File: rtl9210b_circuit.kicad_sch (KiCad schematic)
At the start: 45 parts, among them U1 RTL9210B-CG, U2 W25Q128JVSIQTR, U3 ETA3521FSG_C22362743, X1 X322525MOB4SI

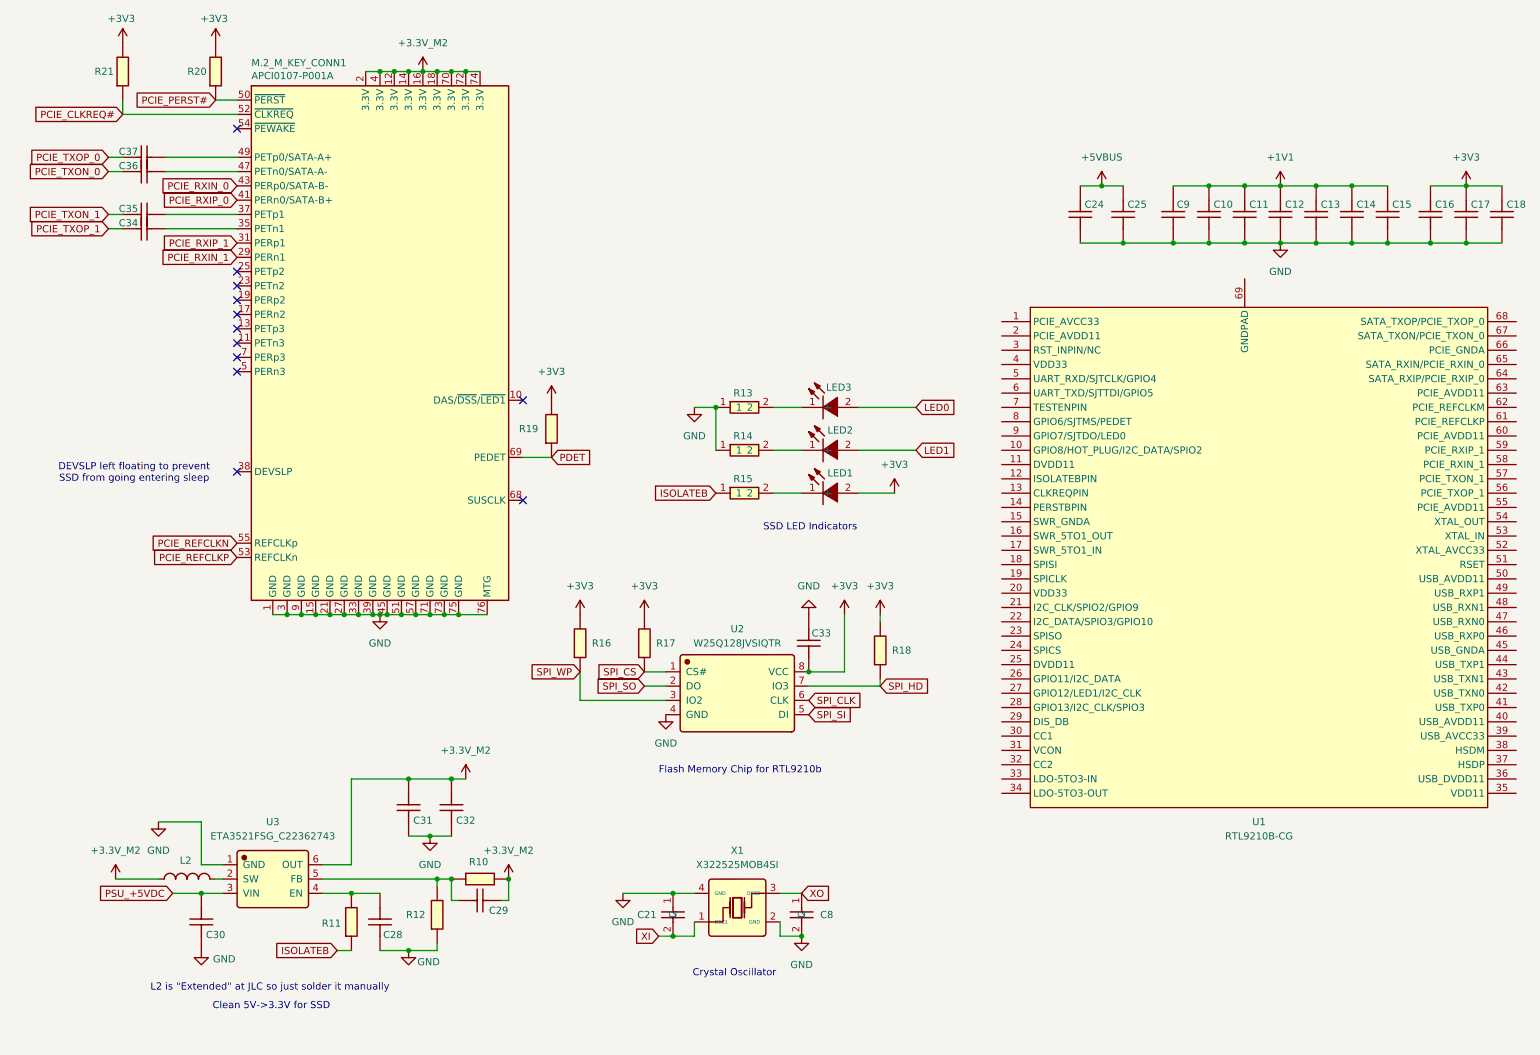
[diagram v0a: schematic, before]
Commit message: Preliminary design of RTL9210b SSD subsystem
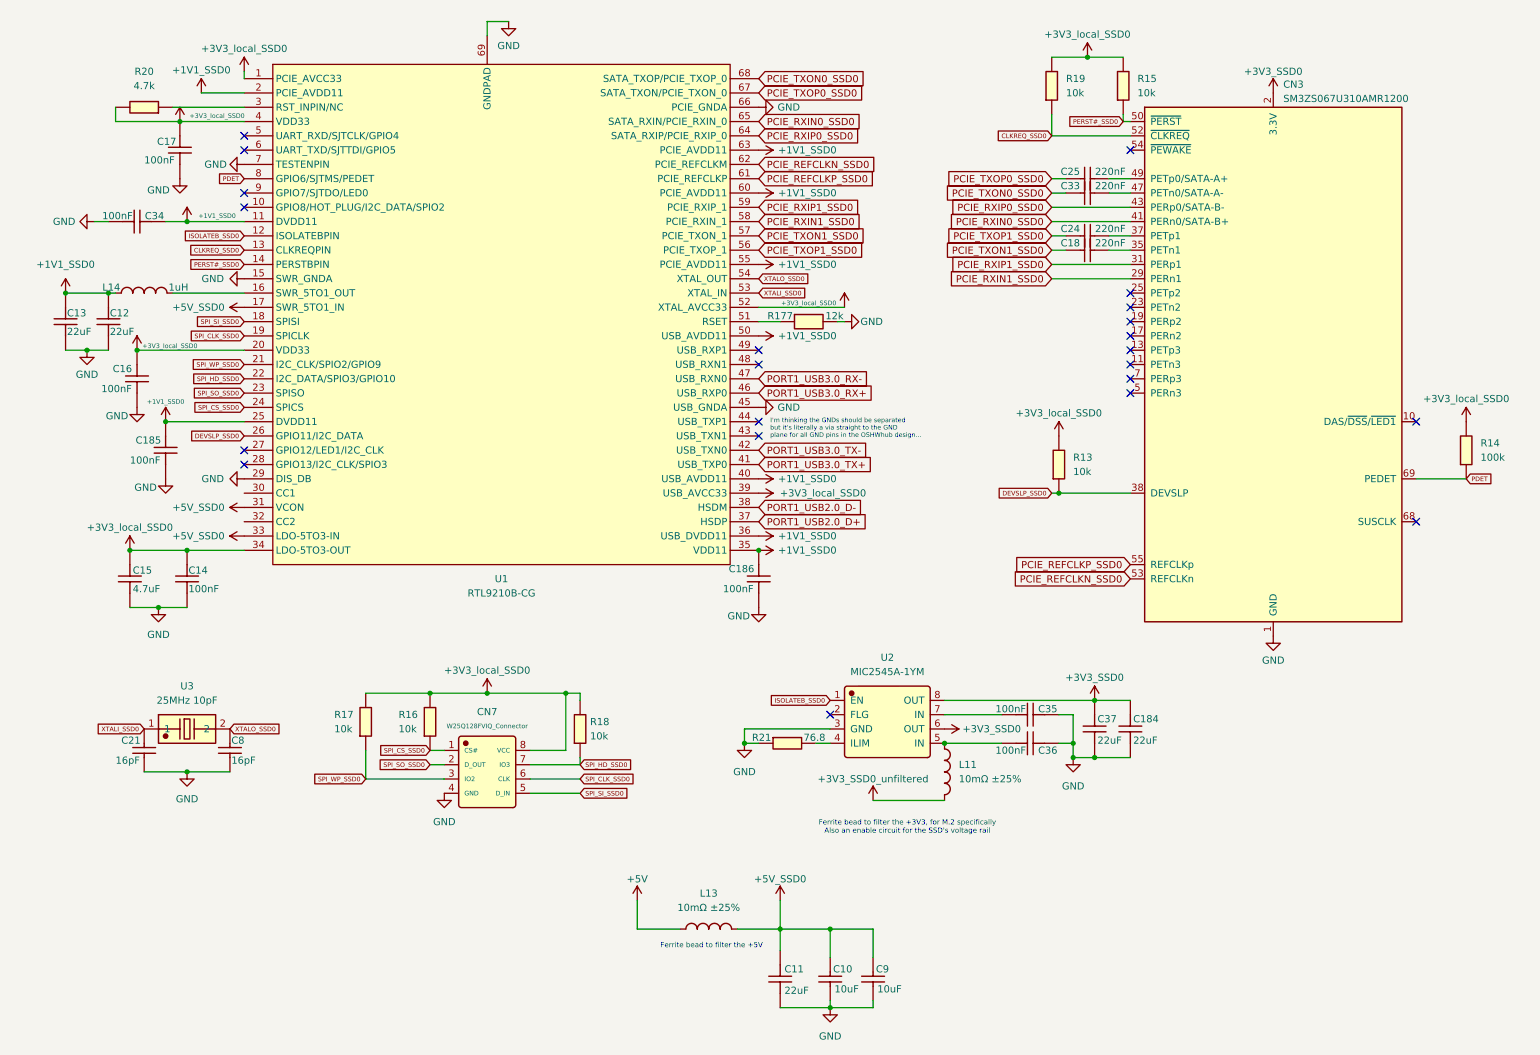
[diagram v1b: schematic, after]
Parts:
- removed C10, C11, C12, C13, C15, C18, C28, C9: CL05B104KB54PNC, Capacitor_SMD:C_0402_1005Metric, symbol JLCImport:CL05B104KB54PNC
- removed C21, C8: 0402CG150J500NT, Capacitor_SMD:C_0402_1005Metric, symbol JLCImport:0402CG150J500NT
- removed C24, C25: CL10A106KP8NNNC, Capacitor_SMD:C_0603_1608Metric, symbol JLCImport:CL10A106KP8NNNC
- removed C29: 0402CG470J500NT, Capacitor_SMD:C_0402_1005Metric, symbol JLCImport:0402CG470J500NT
- removed C30, C31, C32: CL10A226MQ8NRNC, Capacitor_SMD:C_0603_1608Metric, symbol JLCImport:CL10A226MQ8NRNC
- removed C33: CL10A105KB8NNNC, Capacitor_SMD:C_0603_1608Metric, symbol JLCImport:CL10A105KB8NNNC
- removed C34, C35, C36, C37: CL05B224KO5NNNC, Capacitor_SMD:C_0402_1005Metric, symbol JLCImport:CL05B224KO5NNNC
- removed L2: FTC252012S1R0MBCA, TerminalBlock_Phoenix:TerminalBlock_Phoenix_PTSM-0,5-2-2,5-V-SMD_1x02-1MP_P2.50mm_Vertical, symbol JLCImport:FTC252012S1R0MBCA
- removed LED1, LED2, LED3: FC-2012HRK-620D, JLCImport:FC-2012HRK-620D, symbol JLCImport:FC-2012HRK-620D
- removed M.2_M_KEY_CONN1: APCI0107-P001A, JLCImport:APCI0107-P001A, symbol Connector:Bus_M.2_Socket_M
- removed R10: 0603WAF6802T5E, Resistor_SMD:R_0603_1608Metric, symbol JLCImport:0603WAF6802T5E
- removed R11, R19: 0402WGF1003TCE, Resistor_SMD:R_0402_1005Metric, symbol JLCImport:0402WGF1003TCE
- removed R12: 0402WGF1502TCE, Resistor_SMD:R_0402_1005Metric, symbol JLCImport:0402WGF1502TCE
- removed R13, R14, R15: 0603WAF2200T5E, Resistor_SMD:R_0603_1608Metric, symbol JLCImport:0603WAF2200T5E
- removed R20, R21: 0402WGF1002TCE, Resistor_SMD:R_0402_1005Metric, symbol JLCImport:0402WGF1002TCE
- removed U2: W25Q128JVSIQTR, Package_SO:SOIC-8_5.3x5.3mm_P1.27mm, symbol JLCImport:W25Q128JVSIQTR
- removed U3: ETA3521FSG_C22362743, Package_TO_SOT_SMD:SOT-563, symbol JLCImport:ETA3521FSG_C22362743
- removed X1: X322525MOB4SI, Crystal:Crystal_SMD_3225-4Pin_3.2x2.5mm, symbol JLCImport:X322525MOB4SI
- added C10, C9: 10uF, Capacitor_SMD:C_0402_1005Metric, symbol JLCImport:CL05A106MQ5NUNC
- added C11, C12, C13, C184, C37: 22uF, Capacitor_SMD:C_0603_1608Metric, symbol JLCImport:CL10A226MQ8NRNC
- added C15: 4.7uF, Capacitor_SMD:C_0402_1005Metric, symbol JLCImport:CL05A475MP5NRNC
- added C18, C24, C25, C33: 220nF, Capacitor_SMD:C_0402_1005Metric, symbol JLCImport:CL05B224KO5NNNC
- added C185, C186, C34, C35, C36: 100nF, Capacitor_SMD:C_0402_1005Metric, symbol JLCImport:CL05B104KB54PNC
- added C21, C8: 16pF, Capacitor_SMD:C_0402_1005Metric, symbol JLCImport:0402CG160J500NT
- added CN3: SM3ZS067U310AMR1200, JLCImport:SM3ZS067U310AMR1200, symbol JLCImport:SM3ZS067U310AMR1200
- added CN7: W25Q128FVIQ_Connector, JLCImport:H2541FV-C762-2X04P, symbol JLCImport:H2541FV-C762-2X04P
- added L11, L13: 10mΩ ±25%, Inductor_SMD:L_1206_3216Metric, symbol JLCImport:SRLB_1206_600TT60
- added L14: 1uH, TerminalBlock_Phoenix:TerminalBlock_Phoenix_PTSM-0,5-2-2,5-V-SMD_1x02-1MP_P2.50mm_Vertical, symbol JLCImport:PIM252012S1R0MBCA
- added R13, R15, R19: 10k, Resistor_SMD:R_0402_1005Metric, symbol JLCImport:0402WGF1002TCE
- added R14: 100k, Resistor_SMD:R_0402_1005Metric, symbol JLCImport:0402WGF1003TCE
- added R177: 12k, Resistor_SMD:R_0402_1005Metric, symbol JLCImport:CR0402F12K0Q10Z
- added R20: 4.7k, Resistor_SMD:R_0402_1005Metric, symbol JLCImport:0402WGF4701TCE
- added R21: 76.8, Resistor_SMD:R_0402_1005Metric, symbol JLCImport:0402WGF4701TCE
- added U2: MIC2545A-1YM, JLCImport:MIC2545A-1YM, symbol JLCImport:MIC2545A-1YM
- added U3: 25MHz 10pF, JLCImport:25M_10PF_50PPM, symbol JLCImport:25M_10PF_50PPM
- C14, C16, C17: value CL05B104KB54PNC -> 100nF
- R16, R17, R18: value 0402WGF1002TCE -> 10k
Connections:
- net +1V1 is gone; now on net +3V3_local_SSD0: C14.2
- net +3V3 is gone; now on net +3V3_local_SSD0: C16.2, C17.2, R16.2, R17.2, R18.2
- net SPI_CS is gone; now on net SPI_WP_SSD0: R17.1
- net SPI_HD is gone; now on net SPI_HD_SSD0: R18.1
- net SPI_WP is gone; now on net SPI_CS_SSD0: R16.1
- net GND: now also U1.15 (SWR_GNDA), U1.29 (DIS_DB), U1.45 (USB_GNDA), U1.66 (PCIE_GNDA), U1.69 (GNDPAD), U1.7 (TESTENPIN), C10.1, C11.1, C12.1, C13.1, C15.1, C184.1, C185.1, C186.1, C21.1, C34.1, C35.2, C36.2, C37.1, C8.1, C9.1, CN3.1 (GND), CN3.15 (GND), CN3.21 (GND), CN3.27 (GND), CN3.3 (GND), CN3.33 (GND), CN3.39 (GND), CN3.45 (GND), CN3.51 (GND), CN3.57 (GND), CN3.71 (GND), CN3.73 (GND), CN3.75 (GND), CN3.9 (GND), CN7.4 (GND), R177.2, R21.1, U2.3 (GND)
- net PDET: now also U1.8 (GPIO6/SJTMS/PEDET), CN3.69 (PEDET), R14.1
- net +3V3_local_SSD0: now reaches U1.1 (PCIE_AVCC33)
- net +3V3_local_SSD0: now also U1.20 (VDD33), U1.34 (LDO-5TO3-OUT), U1.39 (USB_AVCC33), U1.4 (VDD33), U1.52 (XTAL_AVCC33), C15.2, CN7.8 (VCC), R13.2, R14.2, R15.2, R19.2, R20.2
- net +1V1_SSD0: now reaches U1.11 (DVDD11)
- net +1V1_SSD0: now also U1.2 (PCIE_AVDD11), U1.25 (DVDD11), U1.35 (VDD11), U1.36 (USB_DVDD11), U1.40 (USB_AVDD11), U1.50 (USB_AVDD11), U1.55 (PCIE_AVDD11), U1.60 (PCIE_AVDD11), U1.63 (PCIE_AVDD11), C12.2, C13.2, C185.2, C186.2, C34.2, L14.1
- net ISOLATEB_SSD0: now reaches U1.12 (ISOLATEBPIN)
- net ISOLATEB_SSD0: now also U2.1 (EN)
- net CLKREQ_SSD0: now reaches U1.13 (CLKREQPIN)
- net CLKREQ_SSD0: now also CN3.52 (~{CLKREQ}), R19.1
- net PERST#_SSD0: now reaches U1.14 (PERSTBPIN)
- net PERST#_SSD0: now also CN3.50 (~{PERST}), R15.1
- net at U1.16 (SWR_5TO1_OUT): now also L14.2
- net +5V_SSD0: now reaches U1.17 (SWR_5TO1_IN)
- net +5V_SSD0: now also U1.31 (VCON), U1.33 (LDO-5TO3-IN), C10.2, C11.2, C9.2, L13.2
- net SPI_SI_SSD0: now reaches U1.18 (SPISI)
- net SPI_SI_SSD0: now also CN7.5 (D_IN)
- net SPI_CLK_SSD0: now reaches U1.19 (SPICLK)
- net SPI_CLK_SSD0: now also CN7.6 (CLK)
- net SPI_WP_SSD0: now reaches U1.21 (I2C_CLK/SPIO2/GPIO9)
- net SPI_WP_SSD0: now also CN7.3 (IO2)
- net SPI_HD_SSD0: now reaches U1.22 (I2C_DATA/SPIO3/GPIO10)
- net SPI_HD_SSD0: now also CN7.7 (IO3)
- net SPI_SO_SSD0: now reaches U1.23 (SPISO)
- net SPI_SO_SSD0: now also CN7.2 (D_OUT)
- net SPI_CS_SSD0: now reaches U1.24 (SPICS)
- net SPI_CS_SSD0: now also CN7.1 (CS#)
- net DEVSLP_SSD0: now reaches U1.26 (GPIO11/I2C_DATA)
- net DEVSLP_SSD0: now also CN3.38 (DEVSLP), R13.1
- net at U1.3 (RST_INPIN/NC): now also R20.1
- net PORT1_USB2.0_D+: now reaches U1.37 (HSDP)
- net PORT1_USB2.0_D-: now reaches U1.38 (HSDM)
- net PORT1_USB3.0_TX+: now reaches U1.41 (USB_TXP0)
- net PORT1_USB3.0_TX-: now reaches U1.42 (USB_TXN0)
- net PORT1_USB3.0_RX+: now reaches U1.46 (USB_RXP0)
- net PORT1_USB3.0_RX-: now reaches U1.47 (USB_RXN0)
- net at U1.51 (RSET): now also R177.1
- net XTALI_SSD0: now reaches U1.53 (XTAL_IN)
- net XTALI_SSD0: now also C21.2, U3.1
- net XTALO_SSD0: now reaches U1.54 (XTAL_OUT)
- net XTALO_SSD0: now also C8.2, U3.2
- net PCIE_TXOP1_SSD0: now reaches U1.56 (PCIE_TXOP_1)
- net PCIE_TXOP1_SSD0: now also C24.1
- net PCIE_TXON1_SSD0: now reaches U1.57 (PCIE_TXON_1)
- net PCIE_TXON1_SSD0: now also C18.1
- net PCIE_RXIN1_SSD0: now reaches U1.58 (PCIE_RXIN_1)
- net PCIE_RXIN1_SSD0: now also CN3.29 (PERn1)
- net PCIE_RXIP1_SSD0: now reaches U1.59 (PCIE_RXIP_1)
- net PCIE_RXIP1_SSD0: now also CN3.31 (PERp1)
- net PCIE_REFCLKP_SSD0: now reaches U1.61 (PCIE_REFCLKP)
- net PCIE_REFCLKP_SSD0: now also CN3.55 (REFCLKp)
- net PCIE_REFCLKN_SSD0: now reaches U1.62 (PCIE_REFCLKM)
- net PCIE_REFCLKN_SSD0: now also CN3.53 (REFCLKn)
- net PCIE_RXIP0_SSD0: now reaches U1.64 (SATA_RXIP/PCIE_RXIP_0)
- net PCIE_RXIP0_SSD0: now also CN3.43 (PERp0/SATA-B-)
- net PCIE_RXIN0_SSD0: now reaches U1.65 (SATA_RXIN/PCIE_RXIN_0)
- net PCIE_RXIN0_SSD0: now also CN3.41 (PERn0/SATA-B+)
- net PCIE_TXOP0_SSD0: now reaches U1.67 (SATA_TXON/PCIE_TXON_0)
- net PCIE_TXOP0_SSD0: now also C25.1
- net PCIE_TXON0_SSD0: now reaches U1.68 (SATA_TXOP/PCIE_TXOP_0)
- net PCIE_TXON0_SSD0: now also C33.1
- new net: C33.2, CN3.47 (PETn0/SATA-A-)
- new net: R21.2, U2.4 (ILIM)
- new net: C36.1, L11.1, U2.5 (IN)
- new net: C35.1, U2.7 (IN)
- new net: C24.2, CN3.37 (PETp1)
- new net: C25.2, CN3.49 (PETp0/SATA-A+)
- new net: C18.2, CN3.35 (PETn1)
- new net +3V3_SSD0: C184.2, C37.2, CN3.12 (3.3V), CN3.14 (3.3V), CN3.16 (3.3V), CN3.18 (3.3V), CN3.2 (3.3V), CN3.4 (3.3V), CN3.70 (3.3V), CN3.72 (3.3V), CN3.74 (3.3V), U2.6 (OUT), U2.8 (OUT)
- new net +3V3_SSD0_unfiltered: L11.2
- new net +5V: L13.1
- no-connect marks 12 -> 22
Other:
- note added: "Ferrite bead to filter the +3V3, for M.2 specifically Also an enable circuit for the SSD's voltage rail"
- note added: "Ferrite bead to filter the +5V"
- note added: "I'm thinking the GNDs should be separated but it's literally a via straight to the GND plane for all GND pins in the OSHWhub design..."
- note removed: "Clean 5V->3.3V for SSD"
- note removed: "Crystal Oscillator"
- note removed: "DEVSLP left floating to prevent SSD from going entering sleep"
- note removed: "Flash Memory Chip for RTL9210b"
- note removed: "L2 is "Extended" at JLC so just solder it manually"
- note removed: "SSD LED Indicators"
- moved on the sheet: U1

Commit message: Added CC pull up and pull down resistors for RTL9210b and added power switch for 5V rail for RTL9210b
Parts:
- removed L13: 10mΩ ±25%, Inductor_SMD:L_1206_3216Metric, symbol JLCImport:SRLB_1206_600TT60
- added C187, C188: 100nF, Capacitor_SMD:C_0402_1005Metric, symbol JLCImport:CL05B104KB54PNC
- added L15: 10mΩ ±25%, Inductor_SMD:L_1206_3216Metric, symbol JLCImport:SRLB_1206_600TT60
- added R10, R12: 5.1k, Resistor_SMD:R_0402_1005Metric, symbol JLCImport:0402WGF5101TCE
- added R11: 10k, Resistor_SMD:R_0402_1005Metric, symbol JLCImport:0402WGF1002TCE
- added R180: 76.8, Resistor_SMD:R_0402_1005Metric, symbol JLCImport:0402WGF4701TCE
- added R181: 4.7k, Resistor_SMD:R_0402_1005Metric, symbol JLCImport:0402WGF4701TCE
- added U29: MIC2545A-2YM-TR, JLCImport:MIC2545A-2YM-TR, symbol JLCImport:MIC2545A-2YM-TR
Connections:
- net +5V: now also L15.2
- net +5V_SSD0: now also R11.1, U29.6 (OUT), U29.8 (OUT)
- net GND: now also C187.2, C188.2, R10.1, R12.1, R180.1, R181.2, U29.3 (GND)
- net CC1_SSD0: now reaches U1.30 (CC1)
- net CC1_SSD0: now also R10.2, R11.2
- net CC2_SSD0: now reaches U1.32 (CC2)
- net CC2_SSD0: now also R12.2
- new net: R180.2, U29.4 (ILIM)
- new net: C188.1, L15.1, U29.5 (IN)
- new net: C187.1, U29.7 (IN)
- new net EN#_SSD0: R181.1, U29.1 (EN)
- no-connect marks 22 -> 23
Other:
- note added: "Ferrite bead to filter the +5V Also an enable circuit for the RP2350B"
- note added: "TO: RP2350B"
- note removed: "Ferrite bead to filter the +5V"
- moved on the sheet: C184, C21, C35, C36, C37, C8, CN7, L11, R16, R17, R18, R21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
